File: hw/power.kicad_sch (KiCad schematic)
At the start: 45 parts, among them J9 Expansion, Q8 DMC2053UVT, U1 RT8096B, U2 RT8096B, U3 RT8096B, U5 TPS563249DDC

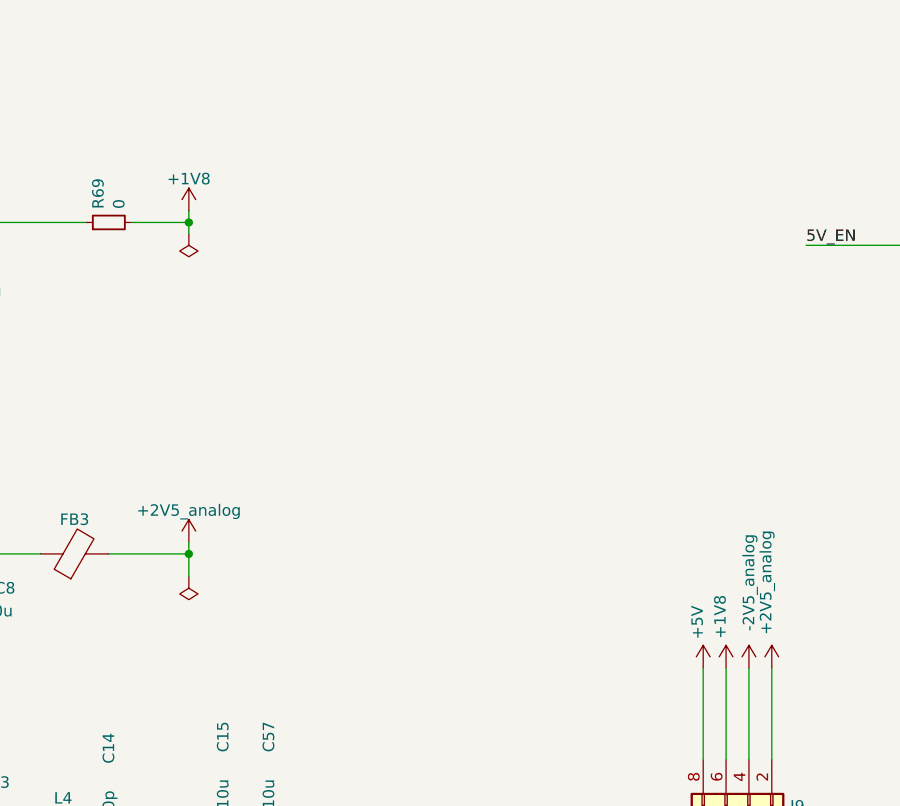
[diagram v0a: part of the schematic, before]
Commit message: moved trion into place; going to 'hide' footprint reference designators...
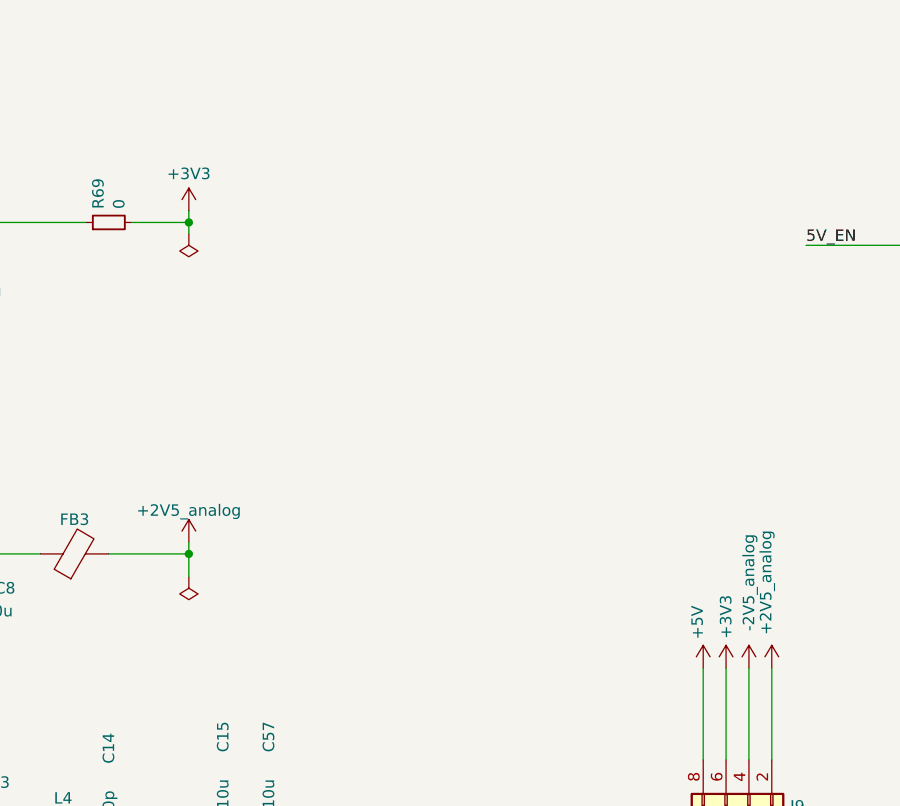
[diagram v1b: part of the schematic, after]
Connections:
- net +1V8 renamed +3V3
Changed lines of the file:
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@@
-    )
-  )
-  (symbol (lib_id "power:+1V8") (at 124.46 68.58 0) (unit 1)
-    (in_bom yes) (on_board yes) (dnp no)
-    (property "Reference" "#PWR0154" (at 124.46 72.39 0)
-      (effects (font (size 1.27 1.27)) hide)
-    )
-    (property "Value" "+1V8" (at 124.46 65.024 0)
-      (effects (font (size 1.27 1.27)))
-    )
-    (property "Footprint" "" (at 124.46 68.58 0)
-      (effects (font (size 1.27 1.27)) hide)
-    )
-    (property "Datasheet" "" (at 124.46 68.58 0)
-      (effects (font (size 1.27 1.27)) hide)
-    )
-    (pin "1")
-    (instances
-      (project "usbadc"
-        (path "/7c8a1f8d-8834-4c9b-aaae-1f231e9b09a1/00000000-0000-0000-0000-00006086f2e3"
-          (reference "#PWR0154") (unit 1)
-        )
-      )
     )
   )
@@
         (path "/7c8a1f8d-8834-4c9b-aaae-1f231e9b09a1/00000000-0000-0000-0000-00006086f2e3"
           (reference "#PWR0157") (unit 1)
-        )
-      )
-    )
-  )
-  (symbol (lib_id "power:+1V8") (at 184.15 119.38 0) (unit 1)
-    (in_bom yes) (on_board yes) (dnp no)
-    (property "Reference" "#PWR0159" (at 184.15 123.19 0)
-      (effects (font (size 1.27 1.27)) hide)
-    )
-    (property "Value" "+1V8" (at 183.515 113.665 90)
-      (effects (font (size 1.27 1.27)))
-    )
-    (property "Footprint" "" (at 184.15 119.38 0)
-      (effects (font (size 1.27 1.27)) hide)
-    )
-    (property "Datasheet" "" (at 184.15 119.38 0)
-      (effects (font (size 1.27 1.27)) hide)
-    )
-    (pin "1")
-    (instances
-      (project "usbadc"
-        (path "/7c8a1f8d-8834-4c9b-aaae-1f231e9b09a1/00000000-0000-0000-0000-00006086f2e3"
-          (reference "#PWR0159") (unit 1)
         )
       )
@@
     )
   )
+  (symbol (lib_id "power:+3V3") (at 124.46 68.58 0) (unit 1)
+    (in_bom yes) (on_board yes) (dnp no) (fields_autoplaced)
+    (property "Reference" "#PWR096" (at 124.46 72.39 0)
+      (effects (font (size 1.27 1.27)) hide)
+    )
+    (property "Value" "+3V3" (at 124.46 64.4469 0)
+      (effects (font (size 1.27 1.27)))
+    )
+    (property "Footprint" "" (at 124.46 68.58 0)
+      (effects (font (size 1.27 1.27)) hide)
+    )
+    (property "Datasheet" "" (at 124.46 68.58 0)
+      (effects (font (size 1.27 1.27)) hide)
+    )
+    (pin "1")
+    (instances
+      (project "usbadc"
+        (path "/7c8a1f8d-8834-4c9b-aaae-1f231e9b09a1/00000000-0000-0000-0000-00006086f2e3"
+          (reference "#PWR096") (unit 1)
+        )
+      )
+    )
+  )
   (symbol (lib_id "Device:C_Small") (at 66.04 140.97 180) (unit 1)
     (in_bom yes) (on_board yes) (dnp no)
@@
         )
       )
+    )
+  )
+  (symbol (lib_id "power:+3V3") (at 184.15 119.38 0) (unit 1)
+    (in_bom yes) (on_board yes) (dnp no)
+    (property "Reference" "#PWR097" (at 184.15 123.19 0)
+      (effects (font (size 1.27 1.27)) hide)
+    )
+    (property "Value" "+3V3" (at 184.15 113.665 90)
+      (effects (font (size 1.27 1.27)))
+    )
+    (property "Footprint" "" (at 184.15 119.38 0)
+      (effects (font (size 1.27 1.27)) hide)
+    )
+    (property "Datasheet" "" (at 184.15 119.38 0)
+      (effects (font (size 1.27 1.27)) hide)
+    )
+    (pin "1")
+    (instances
+      (project "usbadc"
+        (path "/7c8a1f8d-8834-4c9b-aaae-1f231e9b09a1/00000000-0000-0000-0000-00006086f2e3"
+          (reference "#PWR097") (unit 1)
+        )
+      )

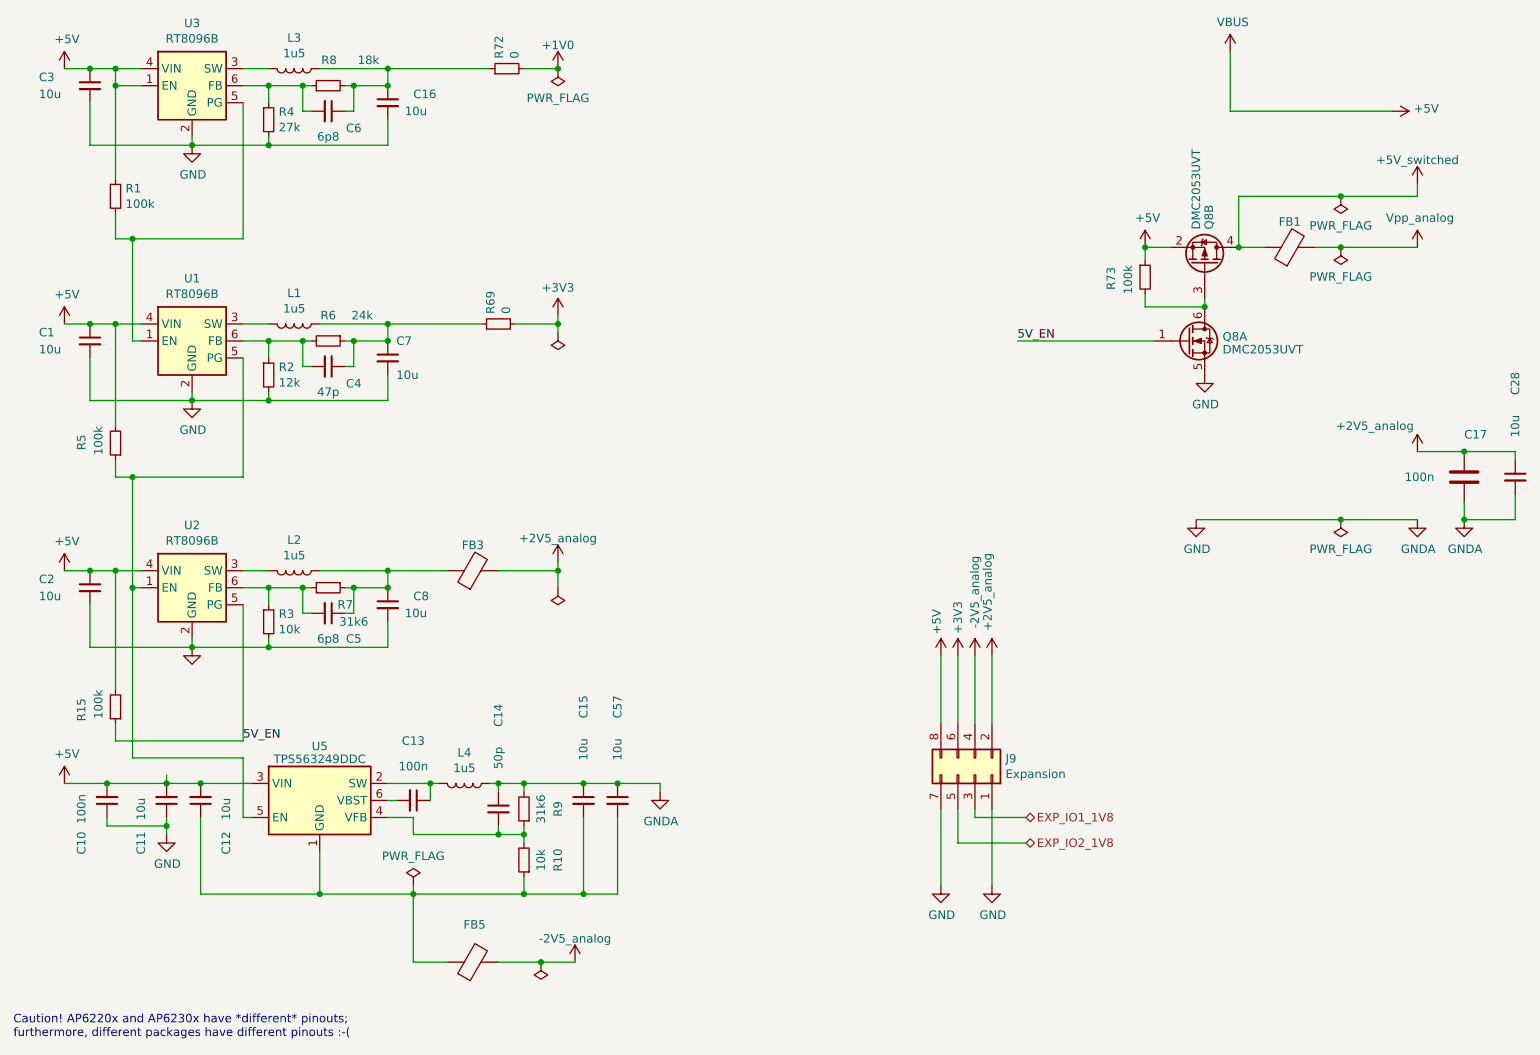
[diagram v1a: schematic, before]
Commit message: layout almost complete with UPLI on the RHS => NO CLOCK INPUT
Have to rework and move the usb transceiver to the left...
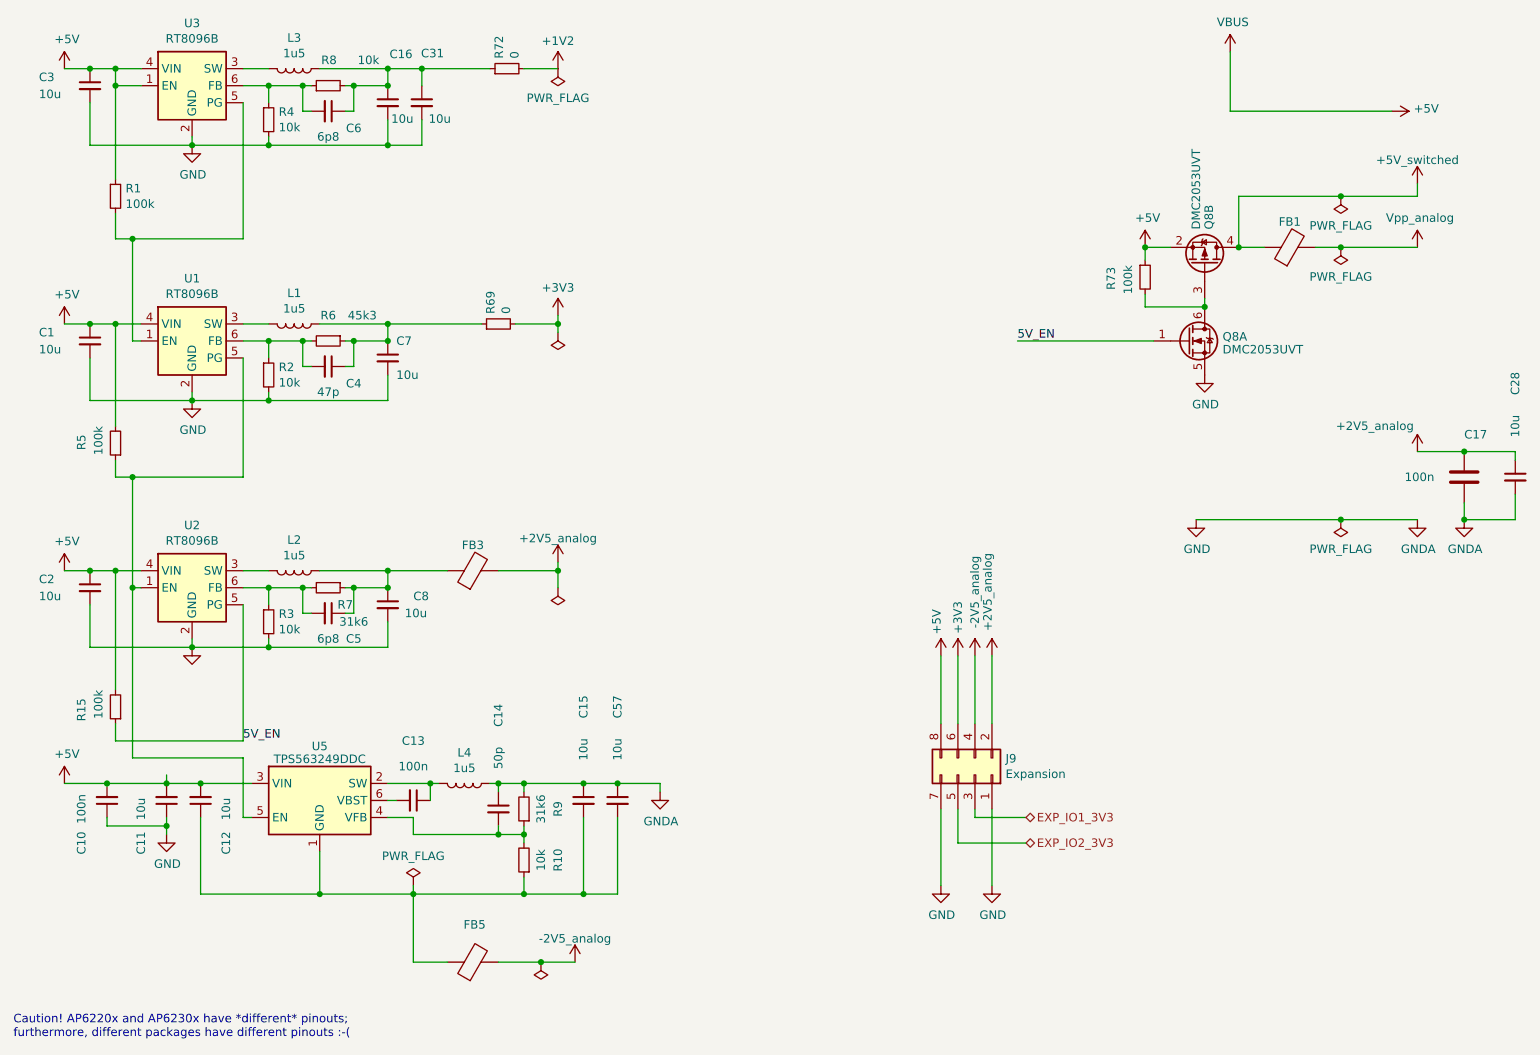
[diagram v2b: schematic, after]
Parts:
- added C31: 10u, Capacitor_SMD:C_1206_3216Metric, symbol Device:C_Small
- R2: value 12k -> 10k
- R4: value 27k -> 10k
- R6: value 24k -> 45k3
- R8: value 18k -> 10k
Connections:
- net GND: now also C31.2
- net at C16.1, C6.1, L3.1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: now also C31.1
- net +1V0 renamed +1V2
- net EXP_IO1_1V8 renamed EXP_IO1_3V3
- net EXP_IO2_1V8 renamed EXP_IO2_3V3
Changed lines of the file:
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@@
 (kicad_sch (version 20230121) (generator eeschema)
   (paper "A4")
-  (junction (at 124.46 31.75) (diameter 0) (color 0 0 0 0)
-  )
   (junction (at 81.28 81.28) (diameter 0) (color 0 0 0 0)
   )
@@
   (junction (at 69.85 81.28) (diameter 0) (color 0 0 0 0)
   )
+  (junction (at 99.06 43.18) (diameter 0) (color 0 0 0 0)
+  )
   (junction (at 99.06 69.85) (diameter 0) (color 0 0 0 0)
   )
@@
   (junction (at 93.98 34.29) (diameter 0) (color 0 0 0 0)
   )
+  (junction (at 104.14 31.75) (diameter 0) (color 0 0 0 0)
+  )
   (junction (at 81.28 118.11) (diameter 0) (color 0 0 0 0)
   )
@@
     (stroke (width 0) (type default))
   )
-  (wire (pts (xy 99.06 31.75) (xy 114.3 31.75))
+  (wire (pts (xy 99.06 31.75) (xy 104.14 31.75))
     (stroke (width 0) (type default))
   )
@@
     (stroke (width 0) (type default))
   )
+  (wire (pts (xy 104.14 39.37) (xy 104.14 43.18))
+    (stroke (width 0) (type default))
+  )
   (wire (pts (xy 71.12 143.51) (xy 71.12 154.94))
     (stroke (width 0) (type default))
@@
     (stroke (width 0) (type default))
   )
+  (wire (pts (xy 104.14 31.75) (xy 104.14 34.29))
+    (stroke (width 0) (type default))
+  )
   (wire (pts (xy 69.85 80.01) (xy 69.85 81.28))
     (stroke (width 0) (type default))
@@
     (stroke (width 0) (type default))
   )
+  (wire (pts (xy 104.14 43.18) (xy 99.06 43.18))
+    (stroke (width 0) (type default))
+  )
   (wire (pts (xy 81.28 116.84) (xy 81.28 118.11))
     (stroke (width 0) (type default))
@@
   )
   (wire (pts (xy 58.42 34.29) (xy 62.23 34.29))
+    (stroke (width 0) (type default))
+  )
+  (wire (pts (xy 104.14 31.75) (xy 114.3 31.75))
     (stroke (width 0) (type default))
   )
@@
     (effects (font (size 1.27 1.27)) (justify left bottom))
   )
-  (hierarchical_label "EXP_IO1_1V8" (shape bidirectional) (at 194.31 143.51 0) (fields_autoplaced)
+  (hierarchical_label "EXP_IO1_3V3" (shape bidirectional) (at 194.31 143.51 0) (fields_autoplaced)
     (effects (font (size 1.27 1.27)) (justify left))
   )
-  (hierarchical_label "EXP_IO2_1V8" (shape bidirectional) (at 194.31 147.32 0) (fields_autoplaced)
+  (hierarchical_label "EXP_IO2_3V3" (shape bidirectional) (at 194.31 147.32 0) (fields_autoplaced)
     (effects (font (size 1.27 1.27)) (justify left))
   )
@@
       (effects (font (size 1.27 1.27)) (justify left))
     )
-    (property "Value" "12k" (at 82.7786 78.613 0)
+    (property "Value" "10k" (at 82.7786 78.613 0)
       (effects (font (size 1.27 1.27)) (justify left))
     )
@@
       (effects (font (size 1.27 1.27)))
     )
-    (property "Value" "24k" (at 95.25 68.58 90)
+    (property "Value" "45k3" (at 95.25 68.58 90)
       (effects (font (size 1.27 1.27)))
     )
@@
   (symbol (lib_id "Device:C_Small") (at 99.06 36.83 0) (unit 1)
     (in_bom yes) (on_board yes) (dnp no)
-    (property "Reference" "C16" (at 102.87 35.56 0)
-      (effects (font (size 1.27 1.27)) (justify left))
-    )
-    (property "Value" "10u" (at 101.6 38.1 0)
+    (property "Reference" "C16" (at 99.314 29.591 0)
+      (effects (font (size 1.27 1.27)) (justify left))
+    )
+    (property "Value" "10u" (at 99.568 39.243 0)
       (effects (font (size 1.27 1.27)) (justify left))
     )
@@
       (effects (font (size 1.27 1.27)) (justify left))
     )
-    (property "Value" "27k" (at 82.7786 40.513 0)
+    (property "Value" "10k" (at 82.7786 40.513 0)
       (effects (font (size 1.27 1.27)) (justify left))
     )
@@
       (effects (font (size 1.27 1.27)) (justify left))
     )
-    (property "Value" "18k" (at 97.79 30.48 90)
+    (property "Value" "10k" (at 97.79 30.48 90)
       (effects (font (size 1.27 1.27)) (justify left))
     )
@@
     )
   )
-  (symbol (lib_id "power:+1V0") (at 124.46 31.75 0) (unit 1)
-    (in_bom yes) (on_board yes) (dnp no) (fields_autoplaced)
-    (property "Reference" "#PWR038" (at 124.46 35.56 0)
-      (effects (font (size 1.27 1.27)) hide)
-    )
-    (property "Value" "+1V0" (at 124.46 28.2481 0)
-      (effects (font (size 1.27 1.27)))
-    )
-    (property "Footprint" "" (at 124.46 31.75 0)
-      (effects (font (size 1.27 1.27)) hide)
-    )
-    (property "Datasheet" "" (at 124.46 31.75 0)
-      (effects (font (size 1.27 1.27)) hide)
-    )
-    (pin "1")
-    (instances
-      (project "usbadc"
-        (path "/7c8a1f8d-8834-4c9b-aaae-1f231e9b09a1/00000000-0000-0000-0000-00006086f2e3"
-          (reference "#PWR038") (unit 1)
-        )
-      )
-    )
-  )
   (symbol (lib_id "fmc:-2V5_analog") (at 186.69 119.38 0) (unit 1)
     (in_bom yes) (on_board yes) (dnp no)
@@
     )
   )
+  (symbol (lib_id "power:+1V2") (at 124.46 31.75 0) (unit 1)
+    (in_bom yes) (on_board yes) (dnp no) (fields_autoplaced)
+    (property "Reference" "#PWR0103" (at 124.46 35.56 0)
+      (effects (font (size 1.27 1.27)) hide)
+    )
+    (property "Value" "+1V2" (at 124.46 27.6169 0)
+      (effects (font (size 1.27 1.27)))
+    )
+    (property "Footprint" "" (at 124.46 31.75 0)
+      (effects (font (size 1.27 1.27)) hide)
+    )
+    (property "Datasheet" "" (at 124.46 31.75 0)
+      (effects (font (size 1.27 1.27)) hide)
+    )
+    (pin "1")
+    (instances
+      (project "usbadc"
+        (path "/7c8a1f8d-8834-4c9b-aaae-1f231e9b09a1/00000000-0000-0000-0000-00006086f2e3"
+          (reference "#PWR0103") (unit 1)
+        )
+      )
+    )
+  )
   (symbol (lib_id "Device:C_Small") (at 128.27 140.97 0) (unit 1)
     (in_bom yes) (on_board yes) (dnp no)
@@
         )
       )
+    )
+  )
+  (symbol (lib_id "Device:C_Small") (at 104.14 36.83 0) (unit 1)
+    (in_bom yes) (on_board yes) (dnp no)
+    (property "Reference" "C31" (at 104.013 29.464 0)
+      (effects (font (size 1.27 1.27)) (justify left))
+    )
+    (property "Value" "10u" (at 105.156 39.243 0)
+      (effects (font (size 1.27 1.27)) (justify left))
+    )
+    (property "Footprint" "Capacitor_SMD:C_1206_3216Metric" (at 104.14 36.83 0)
+      (effects (font (size 1.27 1.27)) hide)
+    )
+    (property "Datasheet" "~" (at 104.14 36.83 0)
+      (effects (font (size 1.27 1.27)) hide)
+    )
+    (property "Part" "" (at 104.14 36.83 0)
+      (effects (font (size 1.27 1.27)) hide)
+    )
+    (property "Manufacturer" "" (at 104.14 36.83 0)
+      (effects (font (size 1.27 1.27)) hide)
+    )
+    (pin "1")
+    (pin "2")
+    (instances
+      (project "usbadc"
+        (path "/7c8a1f8d-8834-4c9b-aaae-1f231e9b09a1/00000000-0000-0000-0000-00006086f2e3"
+          (reference "C31") (unit 1)
+        )
+      )
